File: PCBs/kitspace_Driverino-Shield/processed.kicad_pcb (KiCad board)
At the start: 2 copper layers, 68.6 x 53.3 mm, 58 parts, among them P1 Power, P10 MOT, P11 HALL, P2 Analog, P3 Digital, P4 Digital, P5 CONN_01X01, P6 CONN_01X01, P7 CONN_01X01, P8 CONN_01X01, P9 PWR, U1 MCT8316Z

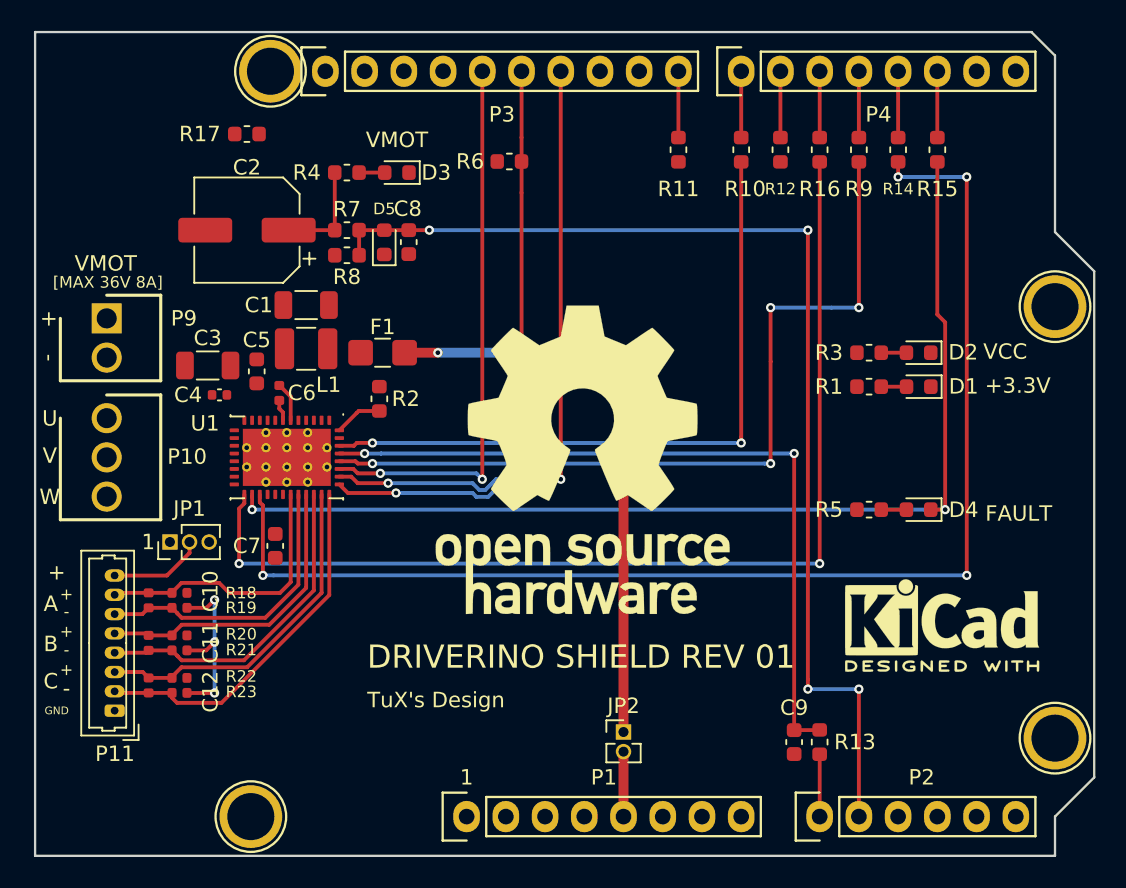
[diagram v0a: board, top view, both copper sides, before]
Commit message: recheck all circuits and clean up fill zone by rerouting the nets using freerouting and manually
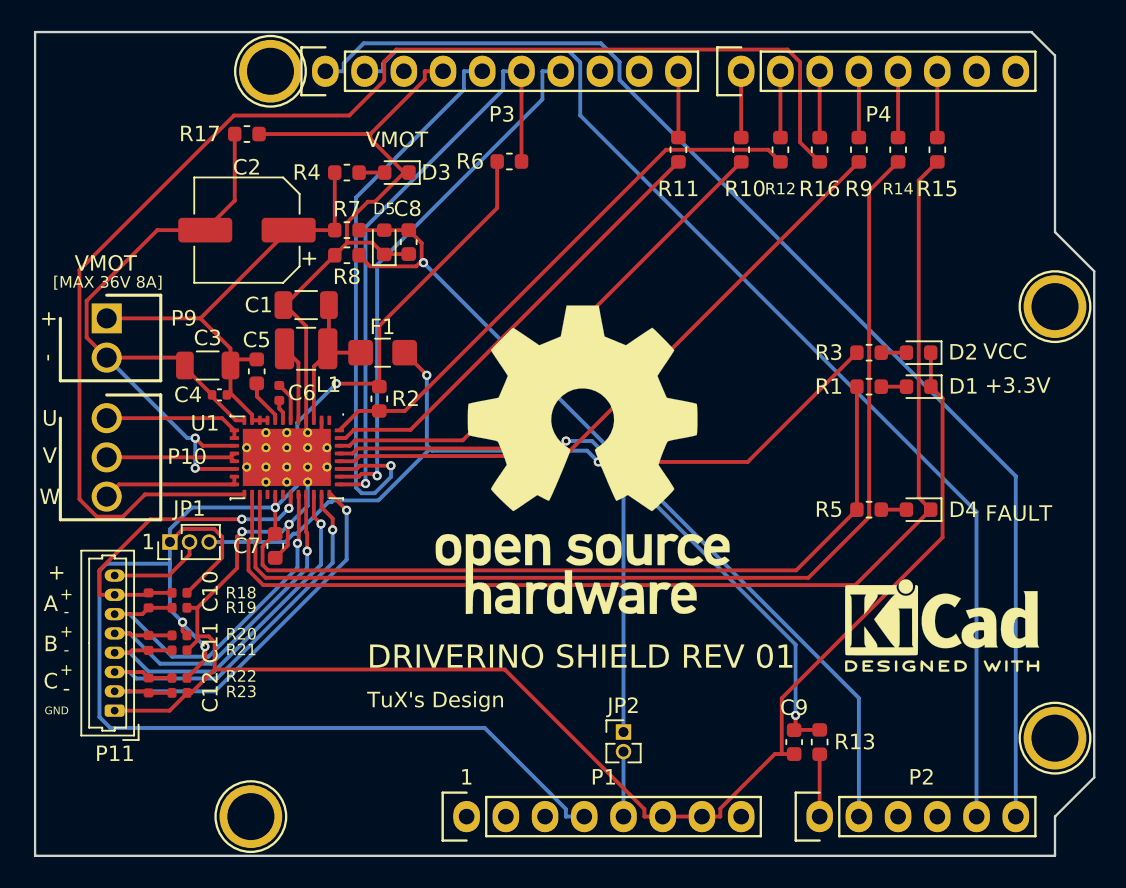
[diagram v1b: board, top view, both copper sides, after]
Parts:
- renumbered REF** to REF**_2
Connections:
- C1 pad 1: (no net) -> GND
- C1 pad 2: (no net) -> /FB
- C2 pad 2: (no net) -> GNDPWR
- C3 pad 1: (no net) -> GNDPWR
- C3 pad 2: (no net) -> +36V
- C4 pad 1: (no net) -> GNDPWR
- C4 pad 2: (no net) -> +36V
- C5 pad 1: (no net) -> Net-(C5-Pad1)
- C5 pad 2: (no net) -> +36V
- C7 pad 1: (no net) -> +3.3V
- C7 pad 2: (no net) -> GND
- C8 pad 1: (no net) -> GND
- C9 pad 1: (no net) -> GND
- D1 pad 1: (no net) -> GND
- D2 pad 1: (no net) -> GND
- D3 pad 1: (no net) -> GND
- D5 pad 1: (no net) -> GND
- F1 pad 2: (no net) -> /FB
- JP1 pad 1: (no net) -> +3.3V
- JP1 pad 3: (no net) -> VCC
- L1 pad 1: (no net) -> /FB
- L1 pad 2: (no net) -> /SW
- P1 pad 4: (no net) -> +3.3V
- P1 pad 6: (no net) -> GND
- P1 pad 7: (no net) -> GND
- P10 pad 1: (no net) -> /U
- P10 pad 2: (no net) -> /V
- P10 pad 3: (no net) -> /W
- P11 pad 1: (no net) -> GND
- P2 pad 5: (no net) -> /A4(SDA)
- P2 pad 6: (no net) -> /A5(SCL)
- P3 pad 1: (no net) -> /A5(SCL)
- P3 pad 2: (no net) -> /A4(SDA)
- P3 pad 4: (no net) -> GND
- P9 pad 1: (no net) -> +36V
- P9 pad 2: (no net) -> GNDPWR
- R1 pad 1: (no net) -> +3.3V
- R11 pad 2: (no net) -> /PWM
- R12 pad 2: (no net) -> /FGOUT
- R17 pad 1: (no net) -> GNDPWR
- R17 pad 2: (no net) -> GND
- R18 pad 2: (no net) -> +3.3V
- R2 pad 1: (no net) -> +3.3V
- R20 pad 2: (no net) -> +3.3V
- R22 pad 2: (no net) -> +3.3V
- R3 pad 1: (no net) -> VCC
- R5 pad 1: (no net) -> +3.3V
- R6 pad 1: (no net) -> +3.3V
- R8 pad 2: (no net) -> GND
- U1 pad 10: (no net) -> +36V
- U1 pad 11: (no net) -> +36V
- U1 pad 12: (no net) -> GNDPWR
- U1 pad 13: (no net) -> /U
- U1 pad 14: (no net) -> /U
- U1 pad 15: (no net) -> GNDPWR
- U1 pad 16: (no net) -> /V
- U1 pad 17: (no net) -> /V
- U1 pad 18: (no net) -> GNDPWR
- U1 pad 19: (no net) -> /W
- U1 pad 2: (no net) -> GND
- U1 pad 20: (no net) -> /W
- U1 pad 25: (no net) -> +3.3V
- U1 pad 3: (no net) -> /FB
- U1 pad 39: (no net) -> /PWM
- U1 pad 4: (no net) -> GND
- U1 pad 41: (no net) -> GND
- U1 pad 5: (no net) -> /SW
- U1 pad 8: (no net) -> Net-(C5-Pad1)
- U1 pad 9: (no net) -> +36V
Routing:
- net +3.3V: track 0.00 -> 159.8 mm, vias 0 -> 4
- net GND: track 11.8 -> 165.7 mm, vias 3 -> 2
- net /A5(SCL): track 0.00 -> 80.1 mm
- net /A4(SDA): track 0.00 -> 74.6 mm
- net GNDPWR: track 0.00 -> 46.7 mm, vias 0 -> 2
- net VCC: track 38.7 -> 72.8 mm
- net /FGOUT: track 3.11 -> 36.4 mm
- net /PWM: track 0.00 -> 29.4 mm
- net +36V: track 6.71 -> 31.8 mm
- net /DRVOFF: track 68.2 -> 87.2 mm, vias 2 -> 0
- net /A1: track 72.0 -> 57.8 mm, vias 4 -> 1
- net /SLEEP: track 82.1 -> 70.3 mm, vias 4 -> 0
- net /CS: track 53.2 -> 41.7 mm, vias 4 -> 0
- net /BRAKE: track 44.3 -> 33.6 mm, vias 2 -> 0
- net /FB: track 0.00 -> 9.99 mm
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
